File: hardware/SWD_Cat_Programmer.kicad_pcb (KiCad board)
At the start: 2 copper layers, 40.5 x 20.1 mm, 28 parts, among them J1 DEBUG_OUTPUT, P1 USB_C_Plug_USB2.0, U1 CH552G, U2 AP2112K-3.3

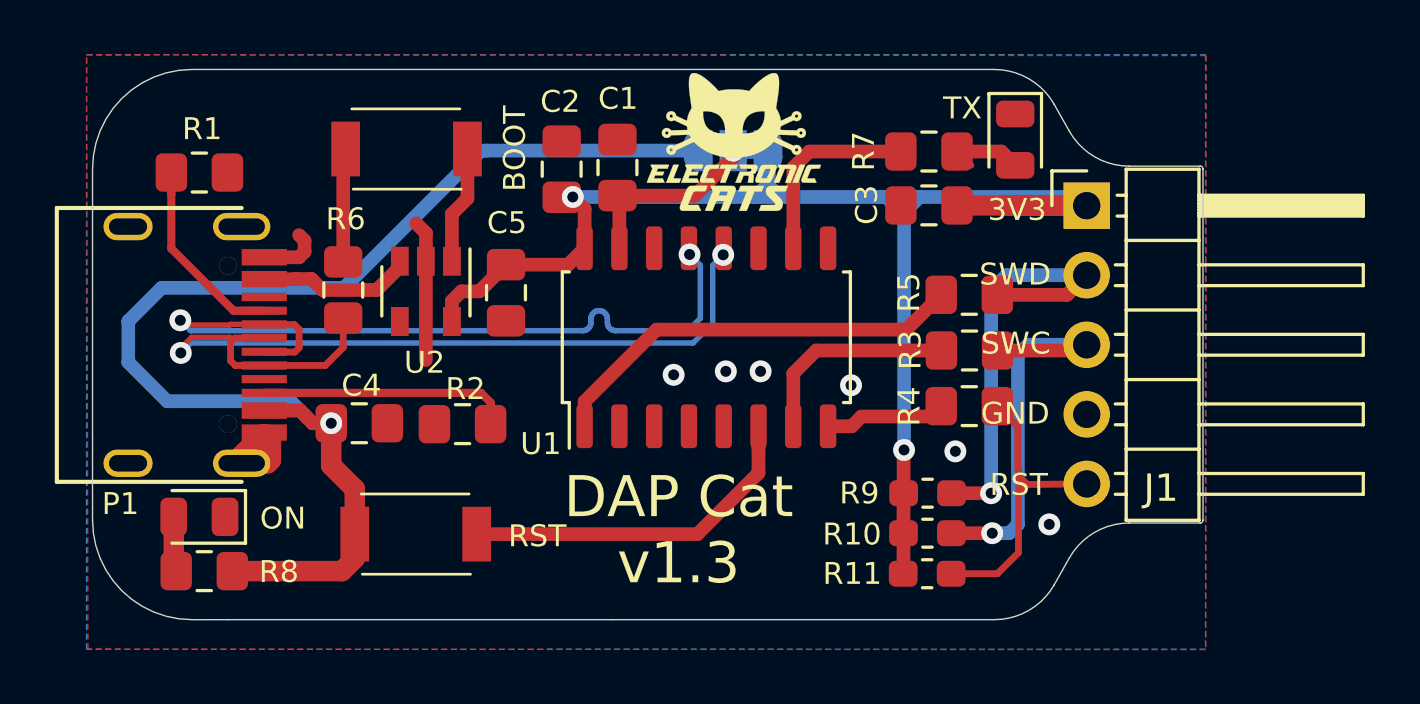
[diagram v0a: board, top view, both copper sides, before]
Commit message: Revert "enhanced routing"
This reverts commit 42d6ad708d969779b1270b3bd74ecf01ee581fea.
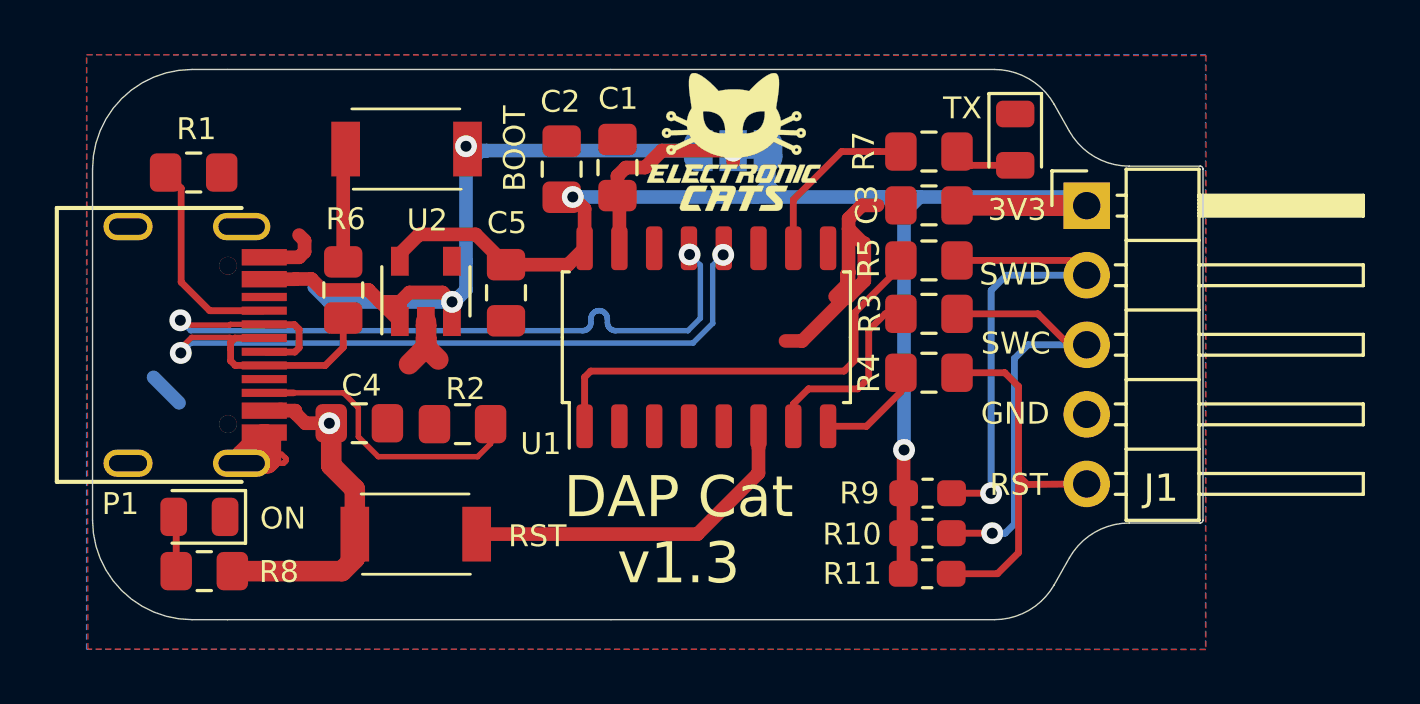
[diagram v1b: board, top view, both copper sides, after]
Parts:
- moved R3 2.00 mm to (161.8, 71.6)
- moved R5 1.94 mm to (161.8, 69.6)
- moved R4 1.91 mm to (161.8, 73.7)
- moved R1 0.21 mm to (135.0, 66.4)
- turned U2 to 90 degrees
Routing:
- net +5V: track 56.4 -> 45.2 mm, vias 1 -> 3
- net GND: track 11.5 -> 22.5 mm, vias 6 -> 0
- net +3V3: track 53.1 -> 57.1 mm
- net /RESET: track 12.2 -> 15.1 mm
- net /SWCLK: track 14.8 -> 16.5 mm
- net Net-(P1-PadB5): track 9.20 -> 10.8 mm
- net /SWDIO: track 16.1 -> 17.5 mm
- net Net-(R5-Pad2): track 15.5 -> 16.3 mm
- net Net-(D1-Pad2): track 3.05 -> 2.33 mm
- net Net-(C1-Pad1): track 7.05 -> 7.72 mm
- net Net-(P1-PadA5): track 7.11 -> 7.71 mm
- net Net-(R3-Pad2): track 7.69 -> 7.12 mm
- net Net-(R4-Pad2): track 4.44 -> 3.88 mm
- net /LED: track 7.12 -> 6.61 mm
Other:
- net class Default removed
